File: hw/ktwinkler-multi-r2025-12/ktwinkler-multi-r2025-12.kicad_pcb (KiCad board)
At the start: 4 copper layers, 64 x 58 mm, 88 parts, among them J1 USB_C_Receptacle_USB2.0_16P, J10 Conn_01x06, J11 Conn_01x02, J12 Connector_HAN_P1, J13 Conn_01x02, J14 Conn_01x02, J15 Conn_01x02, J16 Conn_01x02, J2 Conn_01x02, J3 Conn_01x04, J4 Conn_01x02, J5 Conn_01x03, J6 Conn_01x02, J7 Conn_01x02, J8 Conn_01x02, J9 BWU.FL-IPEX1, Q1 HL3400A, Q3 HL2301A, Q4 HL3400A, SW1 RESET, SW2 BOOT, SW5 MODE, U1 TPS631000DRLR, U2 FM116C, U3 ESP32-C3FH4, U4 T1016H, U5 AD116, U6 Protection_H5VU25UC, U8 CH584F, U9 GM8023B, Y1 40M, Y2 32k, Y4 32k, Y5 32M

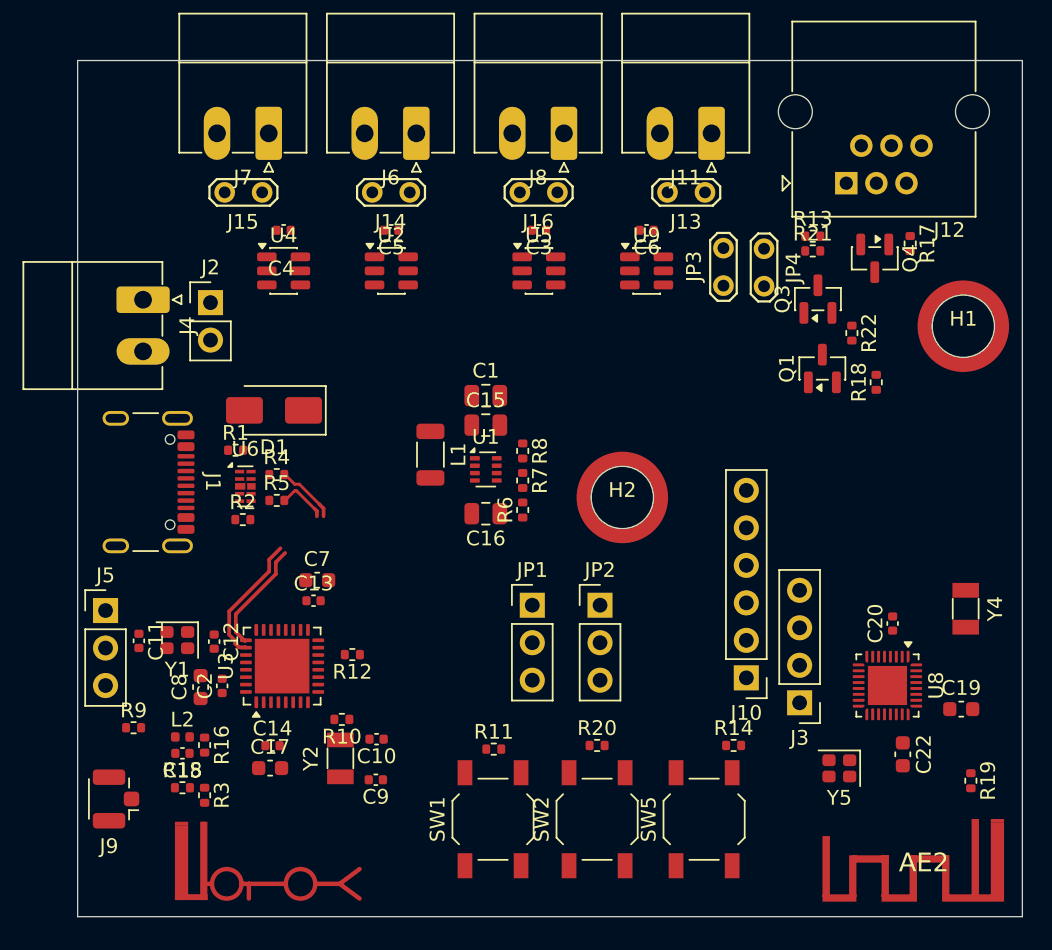
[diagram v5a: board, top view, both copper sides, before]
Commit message: streammmm updates
"complete" apart from finishing those antennas.
needs DRC cleanups on both the wch inv-f and also the yolo-pole.
need to at least _basically_ get the antenna trace basic wdith correct
as well.  yolo is fine, when it's guided yolo, not "lol"
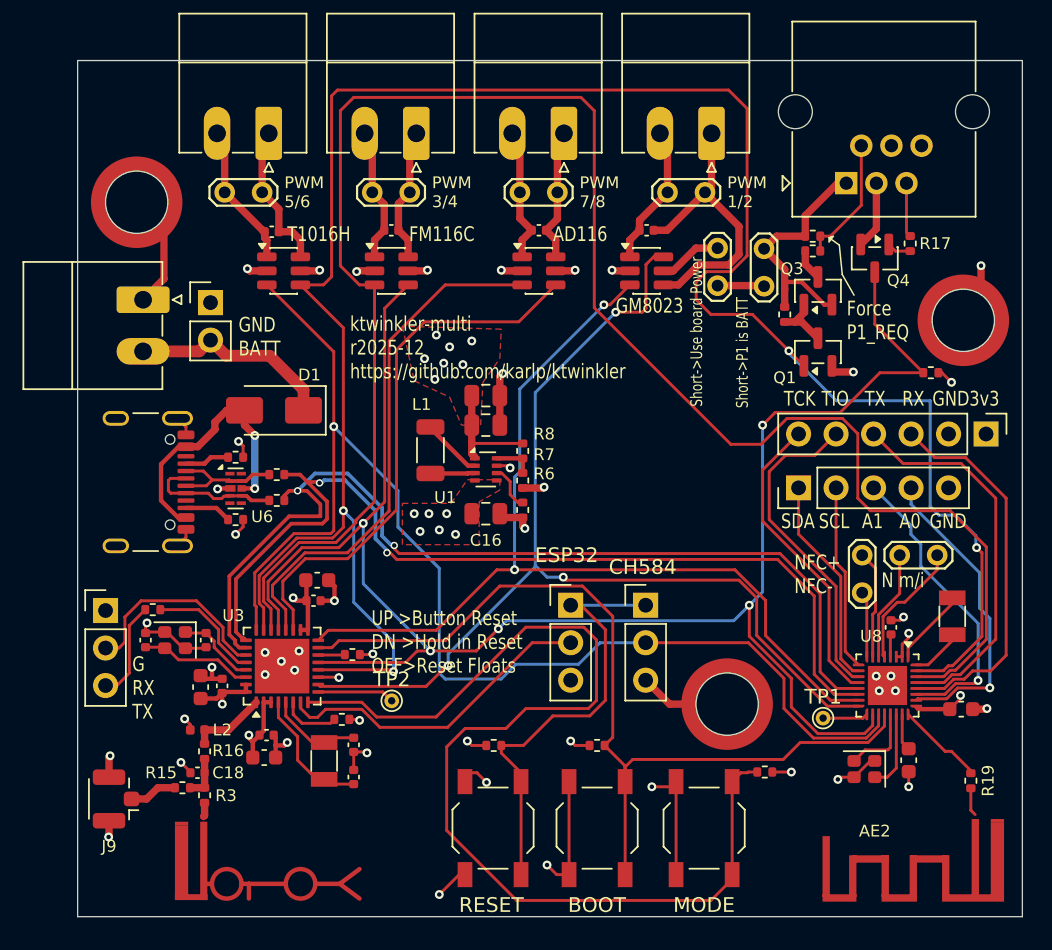
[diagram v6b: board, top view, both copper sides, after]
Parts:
- added H3: Mounting_SMTSO3015CTJ, jlc-extras:Mounting_SMTSO_M3, F.Cu at (160.0, 109.6)
- added J17: Conn_01x02, TestPoint:TestPoint_2Pads_Pitch2.54mm_Drill0.8mm, F.Cu at (158.2, 125.5)
- added J18: Conn_01x02, TestPoint:TestPoint_2Pads_Pitch2.54mm_Drill0.8mm, F.Cu at (153.2, 128.1)
- added TP1: TestPoint, TestPoint:TestPoint_THTPad_D1.0mm_Drill0.5mm, F.Cu at (150.5, 136.6)
- added TP2: TestPoint, TestPoint:TestPoint_THTPad_D1.0mm_Drill0.5mm, F.Cu at (121.3, 135.4)
- J3: value Conn_01x04 -> Conn_01x05; footprint Connector_PinHeader_2.54mm:PinHeader_1x04_P2.54mm_Vertical -> Connector_PinHeader_2.54mm:PinHeader_1x05_P2.54mm_Vertical
- moved H2 38.5 mm to (104.0, 101.6)
- moved H1 30.2 mm to (144.0, 135.6)
- moved J10 23.2 mm to (161.5, 117.3), turned to -90 degrees
- moved J3 14.6 mm to (148.8, 121.0), turned to 90 degrees
- moved R9 8.10 mm to (105.1, 129.2)
- moved R22 4.72 mm to (147.9, 109.2)
- moved R18 3.76 mm to (157.8, 113.2), turned to 180 degrees
- moved JP2 3.09 mm to (138.5, 128.9)
- moved R14 2.77 mm to (146.6, 140.2), turned to 180 degrees
- moved JP1 2.60 mm to (133.4, 128.9)
- moved Y5 1.70 mm to (153.3, 140.0)
- moved C18 1.66 mm to (108.1, 140.2)
- moved C10 1.60 mm to (118.7, 138.4), turned to 90 degrees
- moved C9 1.51 mm to (118.7, 140.5), turned to -90 degrees
- moved Q1 1.15 mm to (150.2, 111.8)
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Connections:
- C11 pad 1: GND -> Net-(U3-XTAL_P)
- C11 pad 2: Net-(U3-XTAL_N) -> GND
- C12 pad 1: Net-(U3-XTAL_P) -> Net-(U3-XTAL_N)
- C5 pad 2: Net-(J6-Pin_2) -> Net-(J14-Pin_2)
- H1 pad 1: unconnected-(H1-Pad1) -> GND
- H2 pad 1: unconnected-(H2-Pad1) -> GND
- J10 pad 2: unconnected-(J10-Pin_2-Pad2) -> GND
- J10 pad 5: /ch584/TIO -> /ch584/TWI_SCL
- J10 pad 6: /ch584/TCK -> /ch584/TWI_SDA
- J14 pad 2: unconnected-(J14-Pin_2-Pad2) -> Net-(J14-Pin_2)
- J3 pad 1: /ch584/TWI_SCL -> /ch584/TIO
- J3 pad 2: /ch584/TWI_SDA -> /ch584/TCK
- J6 pad 2: Net-(J6-Pin_2) -> Net-(J14-Pin_2)
- U2 pad 1: Net-(J6-Pin_2) -> Net-(J14-Pin_2)
- U3 pad 10: /esp32/PWM8 -> /ch584/PWM2
- U3 pad 16: /esp32/PWM7 -> /ch584/PWM1
- U3 pad 19: /ch584/PWM1 -> /esp32/PWM7
- U3 pad 20: /ch584/PWM2 -> /esp32/PWM8
- U3 pad 9: unconnected-(U3-MTMS-Pad9) -> Net-(U3-MTMS)
- U8 pad 17: unconnected-(U8A-PB5_DTR-Pad17) -> Net-(U8A-PB5_DTR)
- U8 pad 26: Net-(J3-Pin_3) -> Net-(J3-Pin_4)
- U8 pad 27: Net-(J3-Pin_4) -> Net-(J3-Pin_3)
- U8 pad 5: unconnected-(U8A-PAB9_NFCI_TMR0_AIN13-Pad5) -> /ch584/nfc_i
- U8 pad 6: unconnected-(U8A-PB8_NFCM-Pad6) -> /ch584/nfc_m
- U8 pad 7: unconnected-(U8B-PB17_NFC+-Pad7) -> /ch584/nfc+
- U8 pad 8: unconnected-(U8B-PB16_NFC--Pad8) -> /ch584/nfc-
- Y1 pad 1: Net-(U3-XTAL_P) -> Net-(U3-XTAL_N)
- Y1 pad 3: Net-(U3-XTAL_N) -> Net-(U3-XTAL_P)
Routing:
- net /ch584/PWM5: track 0.00 -> 148.5 mm, vias 0 -> 4
- net /ch584/PWM4: track 0.00 -> 122.2 mm
- net /ch584/PWM3: track 0.00 -> 119.0 mm, vias 0 -> 5
- net RESET_CH5x: track 0.00 -> 84.6 mm, vias 0 -> 1
- net GND: track 0.00 -> 83.2 mm, vias 0 -> 39
- net /MODE: track 0.00 -> 74.5 mm
- net /ch584/PWM2: track 0.00 -> 72.0 mm, vias 0 -> 3
- net /ch584/PWM1: track 0.00 -> 66.4 mm, vias 0 -> 2
- net GBOOT: track 0.00 -> 61.3 mm
- net USBDP: track 12.3 -> 66.4 mm, vias 0 -> 2
- net USBDN: track 11.8 -> 65.0 mm, vias 0 -> 2
- net /esp32/PWM7: track 0.00 -> 36.7 mm
- net /esp32/PWM8: track 0.00 -> 35.5 mm
- net +3V3: track 0.00 -> 30.6 mm, vias 0 -> 17
- net /RESET_GLOBAL: track 0.00 -> 30.0 mm
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- added copper zone on F.Cu, net +3V3
- added copper zone on In2.Cu, net +3V3
- added copper zone on F.Cu, net +BATT
- added copper zone on In2.Cu, net +BATT
- added copper zone on In1.Cu, net GND
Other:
- board text added: "3v3"
- board text added: "A0"
- board text added: "A1"
- board text added: "AD116"
- board text added: "BOOT"
- board text added: "CH584"
- board text added: "ESP32"
- board text added: "FM116C"
- board text added: "Force P1_REQ"
- board text added: "G RX TX"
- board text added: "GM8023"
- board text added: "GND"
- board text added: "GND BATT"
- board text added: "MODE"
- board text added: "N m/i"
- board text added: "NFC+ NFC-"
- board text added: "PWM 1/2"
- board text added: "PWM 3/4"
- board text added: "PWM 5/6"
- board text added: "PWM 7/8"
- board text added: "RESET"
- board text added: "RX"
- board text added: "SCL"
- board text added: "SDA"
- board text added: "Short->P1 is BATT"
- board text added: "Short->Use board Power"
- board text added: "T1016H"
- board text added: "TCK"
- board text added: "TIO"
- board text added: "TX"
- board text added: "UP >Button Reset DN >Hold in Reset OFF>Reset Floats"
- board text added: "ktwinkler-multi r2025-12 https://github.com/karlp/ktwinkler"

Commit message: attempting to progres towards a build
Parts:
- H1, H2, H3: footprint jlc-extras:Mounting_SMTSO_M3 -> jlc-extras:Mounting_SMTSO_M3_ALT
- moved J9 1.85 mm to (102.6, 140.2)
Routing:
- net GND: track 83.2 -> 81.6 mm, vias 39 -> 70
- added copper zone on F.Cu, net GND

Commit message: hw: save before kicad 10 upgrade
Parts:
- removed J3: Conn_01x05, Connector_PinHeader_2.54mm:PinHeader_1x05_P2.54mm_Vertical
- added J19: Conn_01x06, Connector_PinHeader_2.54mm:PinHeader_1x06_P2.54mm_Vertical, F.Cu at (161.5, 119.8)
- moved R19 0.31 mm to (160.8, 140.8)
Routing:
- net /ch584/TIO: track 14.3 -> 15.4 mm
- net /ch584/TCK: track 12.6 -> 13.7 mm
- net Net-(J19-Pin_3): track 21.1 -> 22.2 mm
- net Net-(J19-Pin_4): track 20.6 -> 21.7 mm
- net /ch584/U_TX: track 26.2 -> 25.6 mm
- net /ch584/PWM4: track 122.2 -> 122.7 mm
- net GND: vias 70 -> 74
